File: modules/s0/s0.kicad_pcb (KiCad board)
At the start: 2 copper layers, 54.6 x 86.4 mm, 74 parts, among them J3 USB_C_Receptacle_USB2.0_14P, J4 BAT_JST_01x02, J5 Conn_Coaxial, J6 Conn_Coaxial, Q1 SS8050, Q2 SS8050, Q3 SS8050, SW1 SW_Push, SW2 SW_Push, U1 BEAGLEBONEBLACK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

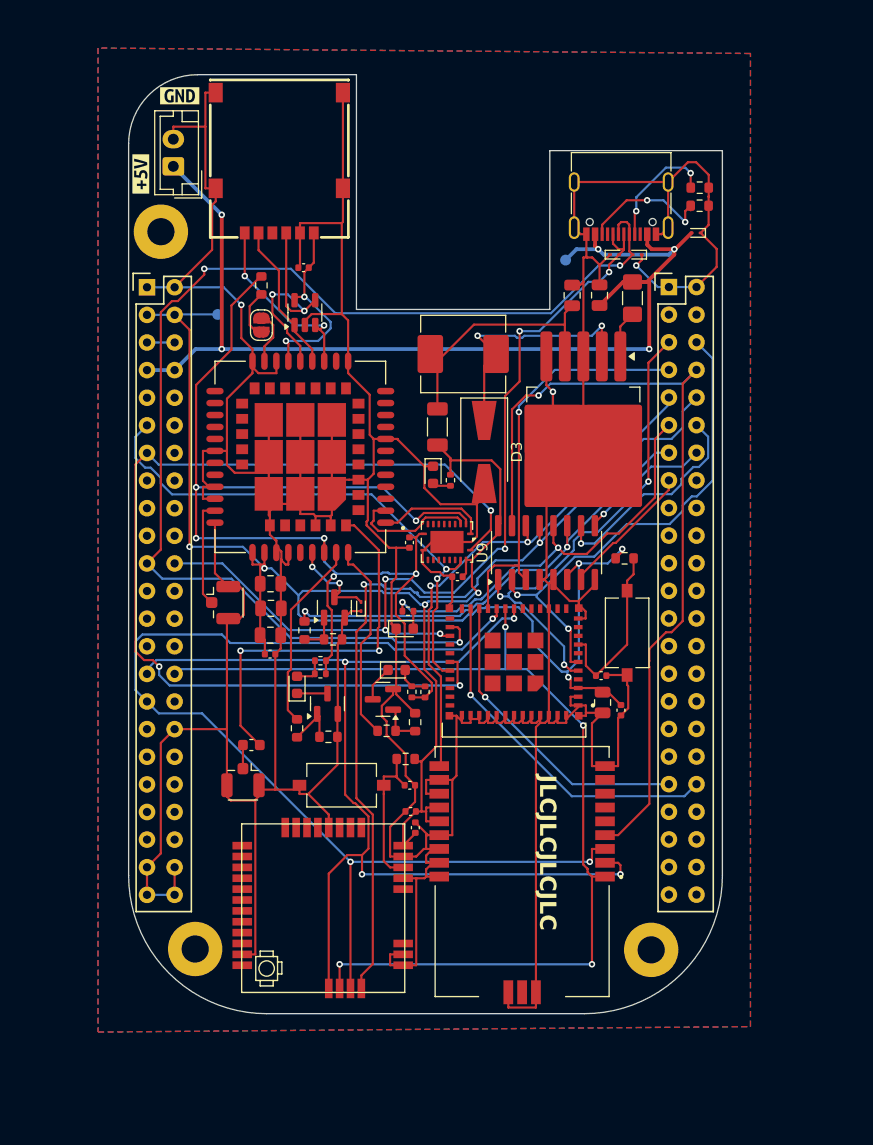
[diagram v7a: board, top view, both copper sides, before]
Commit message: fix: add UART switch for NBIoT and external connector for RS232 connector
Signed-off-by: Rodney Osodo <socials@rodneyosodo.com>
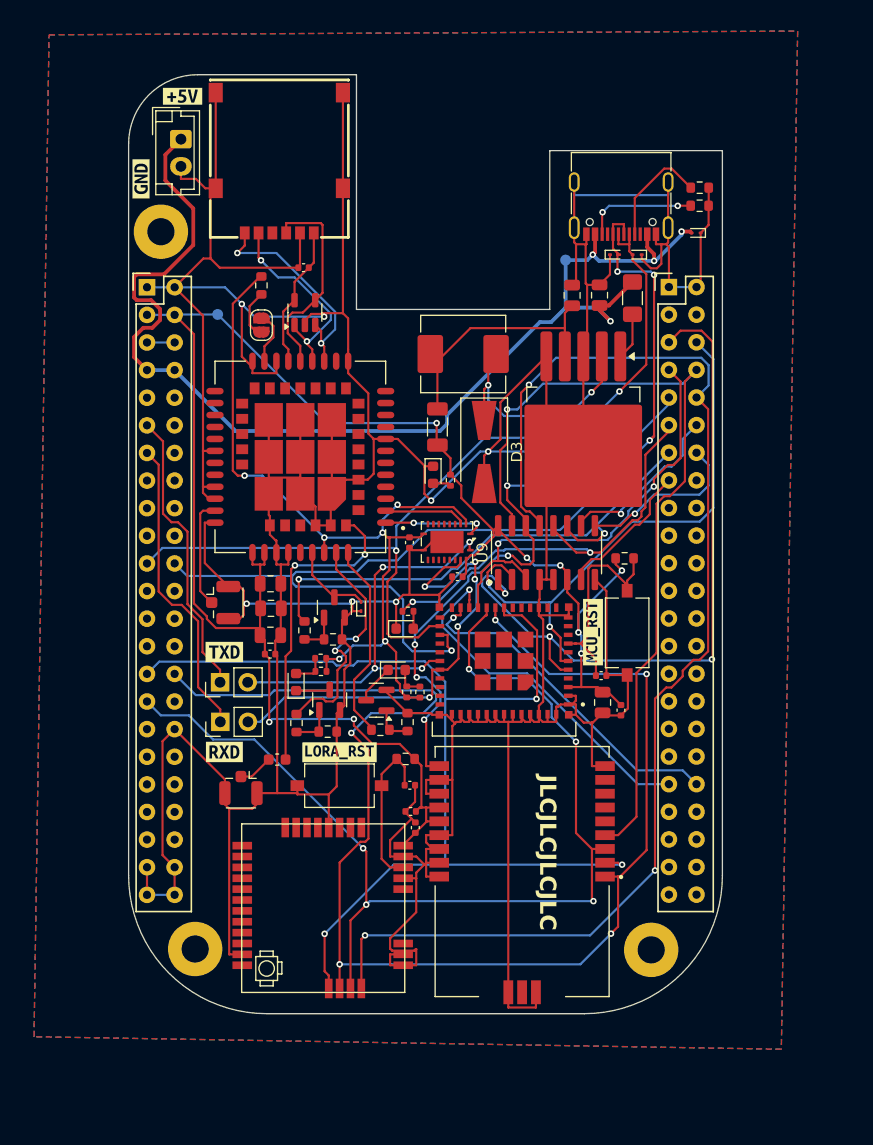
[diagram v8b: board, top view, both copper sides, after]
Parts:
- added J7: Conn_01x02, Connector_PinHeader_2.54mm:PinHeader_1x02_P2.54mm_Vertical, F.Cu at (112.2, 103.5)
- added J8: Conn_01x02, Connector_PinHeader_2.54mm:PinHeader_1x02_P2.54mm_Vertical, F.Cu at (112.2, 99.8)
- added kibuzzard-682321D3: G***, kibuzzard-682321D3, F.Cu at (112.6, 106.2)
- added kibuzzard-682321E3: G***, kibuzzard-682321E3, F.Cu at (112.6, 97.0)
- added kibuzzard-6823224D: G***, kibuzzard-6823224D, F.Cu at (123.2, 106.3)
- added kibuzzard-68232263: G***, kibuzzard-68232263, F.Cu at (146.5, 95.2)
- moved kibuzzard-67D322D7 8.43 mm to (105.0, 53.5), turned to 90 degrees
- moved kibuzzard-67D322D0 8.12 mm to (108.8, 45.9), turned to 0 degrees
- moved C10 2.72 mm to (117.5, 106.9)
- moved J4 2.60 mm to (108.6, 49.9), turned to -90 degrees
- moved U6 0.92 mm to (138.3, 97.9)
- moved J5 0.75 mm to (114.1, 109.5)
- moved R12 0.70 mm to (129.5, 103.5)
- moved Q3 0.61 mm to (126.6, 101.5)
- moved R7 0.57 mm to (127.0, 104.2)
- moved R6 0.49 mm to (119.2, 103.6)
- moved R11 0.48 mm to (122.1, 104.4)
- moved R14 0.47 mm to (129.4, 100.7)
- moved R10 0.47 mm to (130.6, 100.7)
- moved Q2 0.41 mm to (122.3, 101.4)
- moved D7 0.27 mm to (119.2, 99.8)
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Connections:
- U1 pad P9_11: SIM7080G_RXD -> Net-(J8-Pin_1)
- U1 pad P9_13: SIM7080G_TXD -> Net-(J7-Pin_1)
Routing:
- net SIM7080G_TXD: track 91.5 -> 37.8 mm, vias 3 -> 4
- net LORA_CS: track 80.3 -> 116.2 mm, vias 2 -> 3
- net MISO: track 94.4 -> 130.0 mm, vias 4 -> 5
- net +1V8: track 107.6 -> 75.8 mm
- net USB_D-: track 111.8 -> 83.0 mm, vias 3 -> 2
- net Net-(J7-Pin_1): track 0.00 -> 28.0 mm
- net Net-(J8-Pin_1): track 0.00 -> 26.8 mm
- net MUX1: track 44.1 -> 67.6 mm
- net USB_D+: track 83.1 -> 99.6 mm, vias 6 -> 4
- net +3V3: track 179.7 -> 163.4 mm, vias 7 -> 8
- net GND: track 619.4 -> 629.9 mm, vias 3 -> 7
- net +5V: track 100.8 -> 109.2 mm, vias 5 -> 4
- net WMBUS_SDN: track 48.3 -> 56.6 mm, vias 2 -> 5
- net SCK: track 102.9 -> 96.3 mm, vias 3 -> 5
- net GNSS_ANT: track 35.5 -> 28.9 mm
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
